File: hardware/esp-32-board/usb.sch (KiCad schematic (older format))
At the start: 14 parts, among them J5 USB_B_Micro, Q1 BCR129S, U2 USBLC6-2SC6, U3 FT232RL

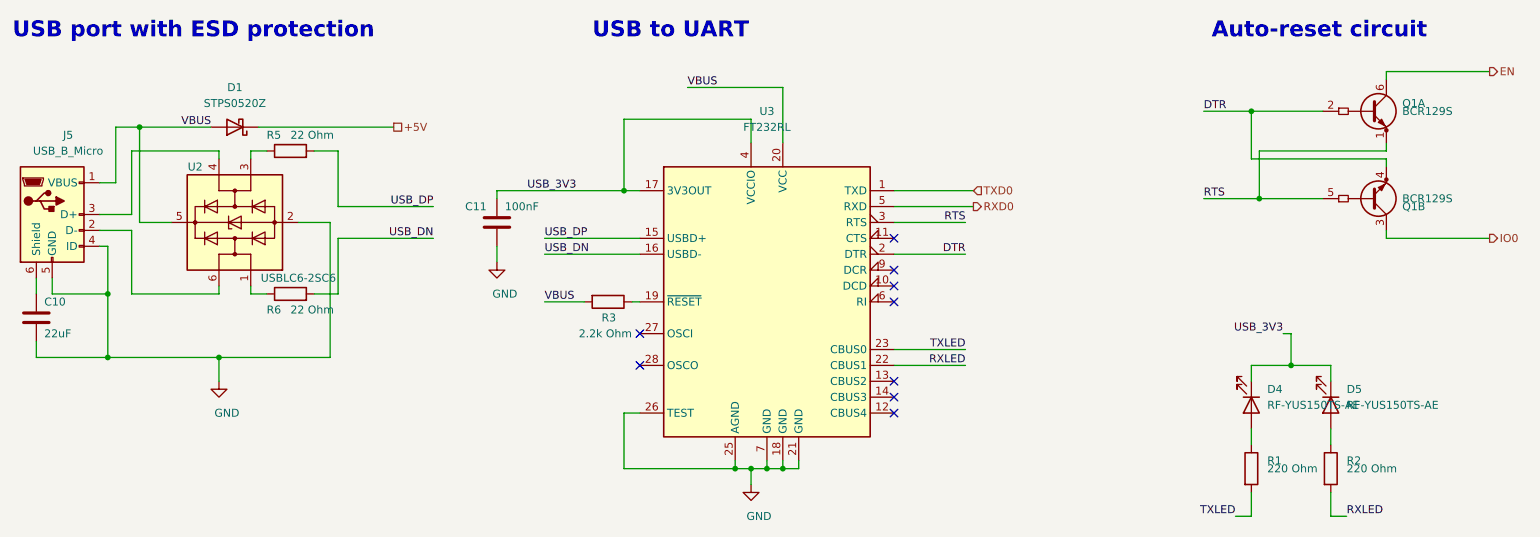
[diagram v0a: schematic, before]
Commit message: Reannotate schematic
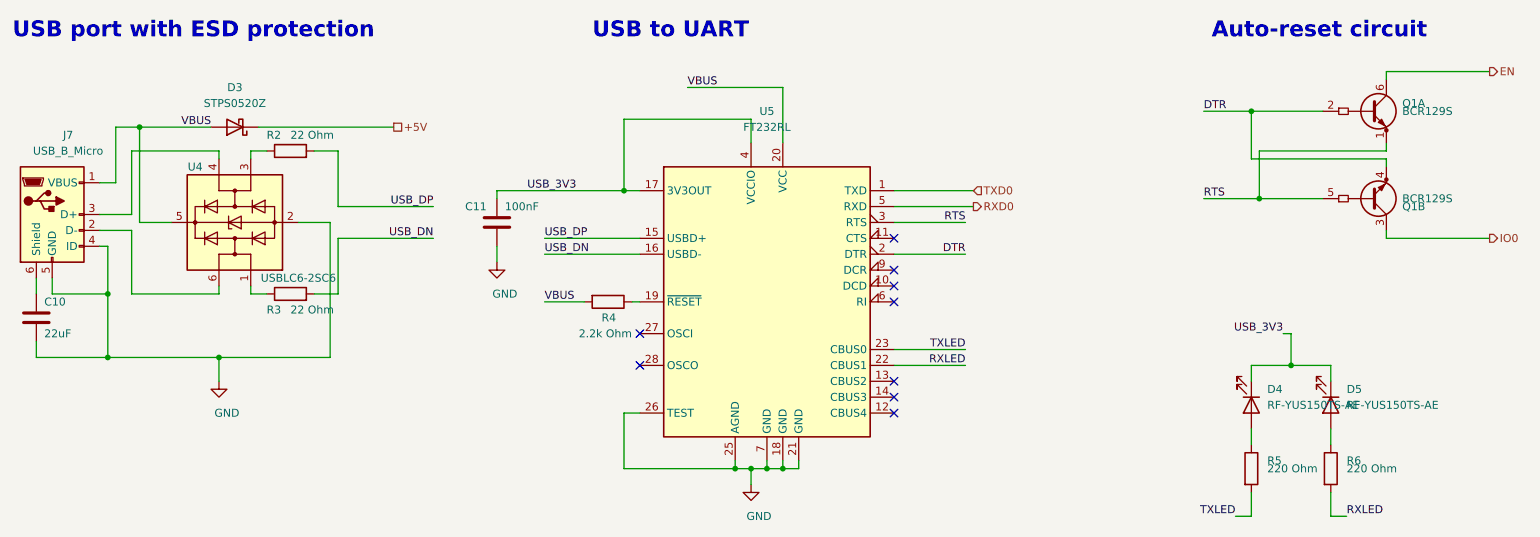
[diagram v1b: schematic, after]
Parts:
- renumbered D1 to D3, J5 to J7, R5 to R2, R6 to R3, R3 to R4, R1 to R5, R2 to R6, U2 to U4, U3 to U5
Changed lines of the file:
@@
 P 5050 3300
 AR Path="/5FFBA107" Ref="R?"  Part="1"
-AR Path="/5FF73D59/5FFBA107" Ref="R3"  Part="1"
-F 0 "R3" V 5150 3350 50  0000 R CNN
+AR Path="/5FF73D59/5FFBA107" Ref="R4"  Part="1"
+F 0 "R4" V 5150 3350 50  0000 R CNN
 F 1 "2.2k Ohm" V 5250 3450 50  0000 R CNN
 F 2 "Resistor_SMD:R_0805_2012Metric_Pad1.20x1.40mm_HandSolder" V 4980 3300 50  0001 C CNN
@@
 P 1550 2750
 AR Path="/5FFC9948" Ref="J?"  Part="1"
-AR Path="/5FF73D59/5FFC9948" Ref="J5"  Part="1"
-F 0 "J5" H 1650 3250 50  0000 C CNN
+AR Path="/5FF73D59/5FFC9948" Ref="J7"  Part="1"
+F 0 "J7" H 1650 3250 50  0000 C CNN
 F 1 "USB_B_Micro" H 1650 3150 50  0000 C CNN
 F 2 "Connector_USB:USB_Micro-B_Molex-105017-0001" H 1700 2700 50  0001 C CNN
@@
 AR Path="/5FB2216A" Ref="D?"  Part="1"
 AR Path="/5FF6344B/5FB2216A" Ref="D?"  Part="1"
-AR Path="/5FF73D59/5FB2216A" Ref="D1"  Part="1"
-F 0 "D1" H 2700 1950 50  0000 C CNN
+AR Path="/5FF73D59/5FB2216A" Ref="D3"  Part="1"
+F 0 "D3" H 2700 1950 50  0000 C CNN
 F 1 "STPS0520Z" H 2700 2050 50  0000 C CNN
 F 2 "Diode_SMD:D_SOD-123" H 2700 2200 50  0001 C CNN
@@
 	1450 3150 1450 3250
 $Comp
-L Power_Protection:USBLC6-2SC6 U2
+L Power_Protection:USBLC6-2SC6 U4
 U 1 1 601988F8
 P 2700 2800
-F 0 "U2" V 3050 3050 50  0000 C CNN
+F 0 "U4" V 3050 3050 50  0000 C CNN
 F 1 "USBLC6-2SC6" V 2350 2400 50  0000 C CNN
 F 2 "Package_TO_SOT_SMD:SOT-23-6" H 2700 2300 50  0001 C CNN
@@
 P 3050 2350
 AR Path="/5FC3959C" Ref="R?"  Part="1"
-AR Path="/5FF73D59/5FC3959C" Ref="R5"  Part="1"
-F 0 "R5" V 3150 2500 50  0000 R CNN
+AR Path="/5FF73D59/5FC3959C" Ref="R2"  Part="1"
+F 0 "R2" V 3150 2500 50  0000 R CNN
 F 1 "22 Ohm" V 3150 2350 50  0000 R CNN
 F 2 "Resistor_SMD:R_0805_2012Metric_Pad1.20x1.40mm_HandSolder" V 2980 2350 50  0001 C CNN
@@
 P 3050 3250
 AR Path="/5FC43B6A" Ref="R?"  Part="1"
-AR Path="/5FF73D59/5FC43B6A" Ref="R6"  Part="1"
-F 0 "R6" V 2950 3400 50  0000 R CNN
+AR Path="/5FF73D59/5FC43B6A" Ref="R3"  Part="1"
+F 0 "R3" V 2950 3400 50  0000 R CNN
 F 1 "22 Ohm" V 2950 3250 50  0000 R CNN
 F 2 "Resistor_SMD:R_0805_2012Metric_Pad1.20x1.40mm_HandSolder" V 2980 3250 50  0001 C CNN
@@
 	6150 1950 6150 2300
 $Comp
-L Interface_USB:FT232RL U3
+L Interface_USB:FT232RL U5
 U 1 1 5FE99968
 P 6050 3300
-F 0 "U3" H 6050 4500 50  0000 C CNN
+F 0 "U5" H 6050 4500 50  0000 C CNN
 F 1 "FT232RL" H 6050 4400 50  0000 C CNN
 F 2 "Package_SO:SSOP-28_5.3x10.2mm_P0.65mm" H 7150 2400 50  0001 C CNN
@@
 	9350 3700 9600 3700
 $Comp
-L Device:R R1
+L Device:R R5
 U 1 1 5FFD83B8
 P 9100 4350
-F 0 "R1" H 9200 4400 50  0000 L CNN
+F 0 "R5" H 9200 4400 50  0000 L CNN
 F 1 "220 Ohm" H 9200 4350 50  0000 L CNN
 F 2 "Resistor_SMD:R_0805_2012Metric_Pad1.20x1.40mm_HandSolder" V 9030 4350 50  0001 C CNN
@@
 $EndComp
 $Comp
-L Device:R R2
+L Device:R R6
 U 1 1 5FFDD2E6
 P 9600 4350
-F 0 "R2" H 9700 4400 50  0000 L CNN
+F 0 "R6" H 9700 4400 50  0000 L CNN
 F 1 "220 Ohm" H 9700 4350 50  0000 L CNN
 F 2 "Resistor_SMD:R_0805_2012Metric_Pad1.20x1.40mm_HandSolder" V 9530 4350 50  0001 C CNN
